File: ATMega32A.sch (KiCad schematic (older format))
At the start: 17 parts, among them J201 AVR-ISP-6, J202 UART, U201 ATmega32A-AU, Y201 16MHz

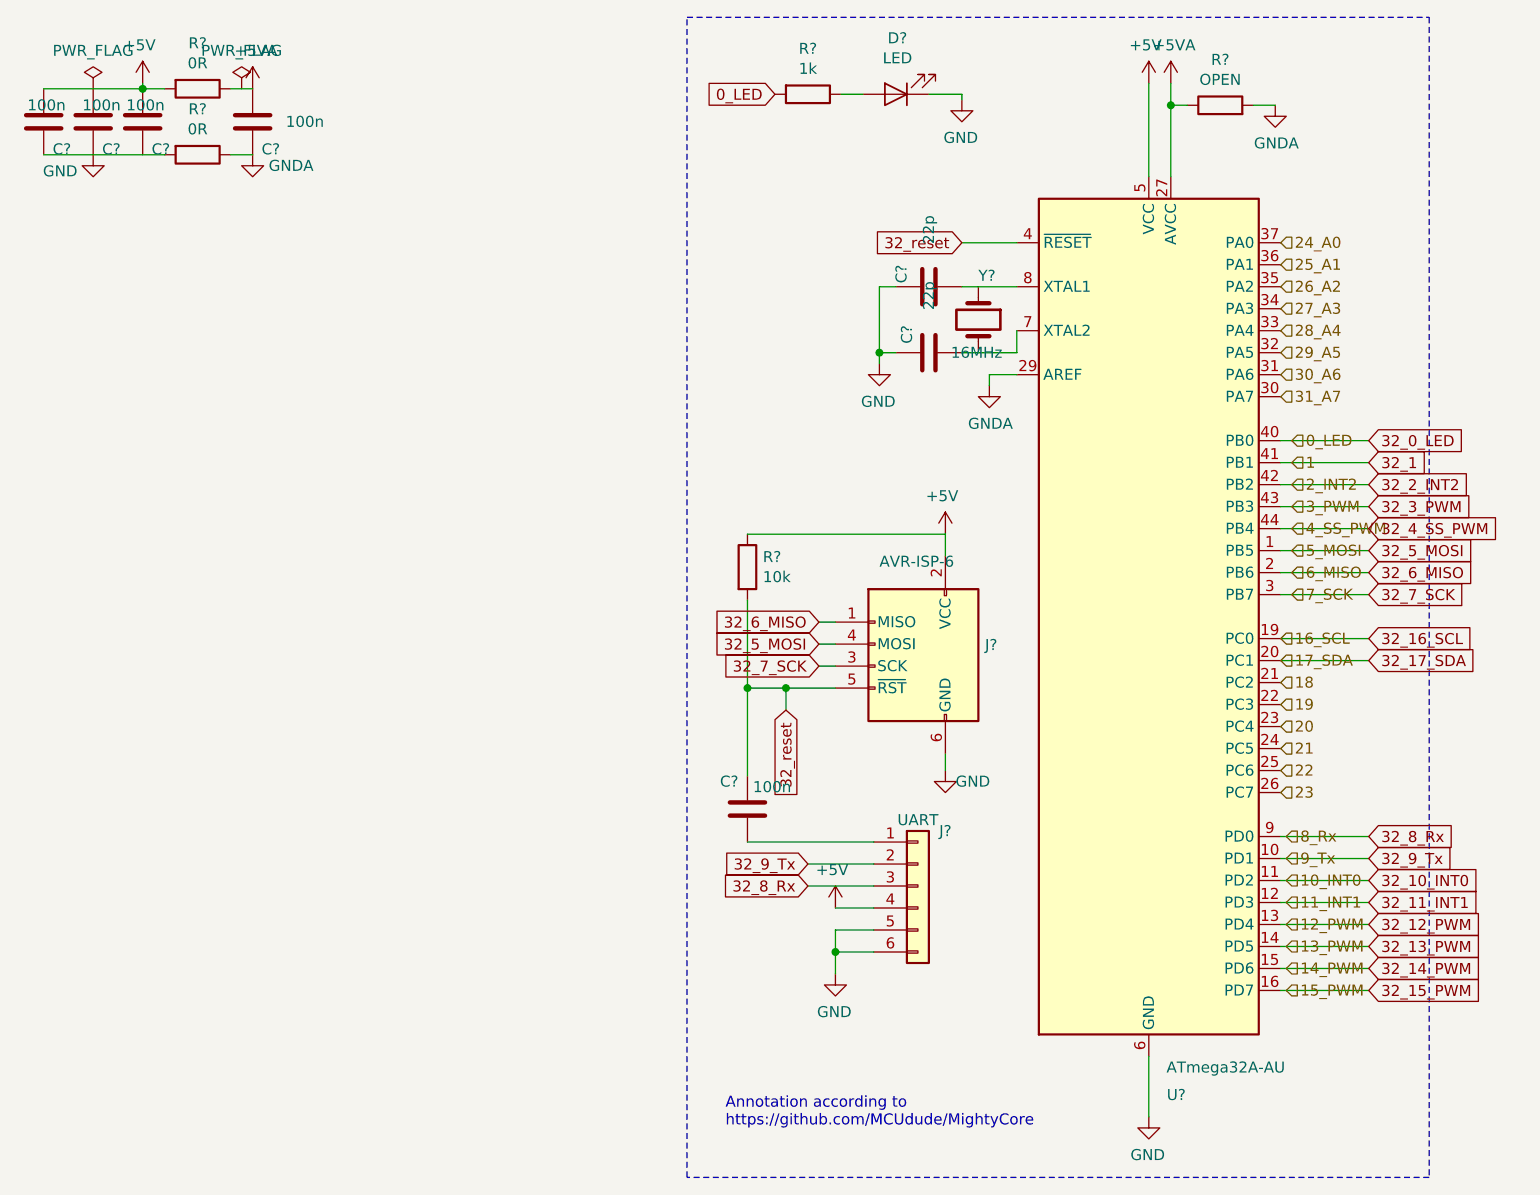
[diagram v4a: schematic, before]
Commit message: Intersheet cleanup
Footprints and cleanup naming on global labels between sheets
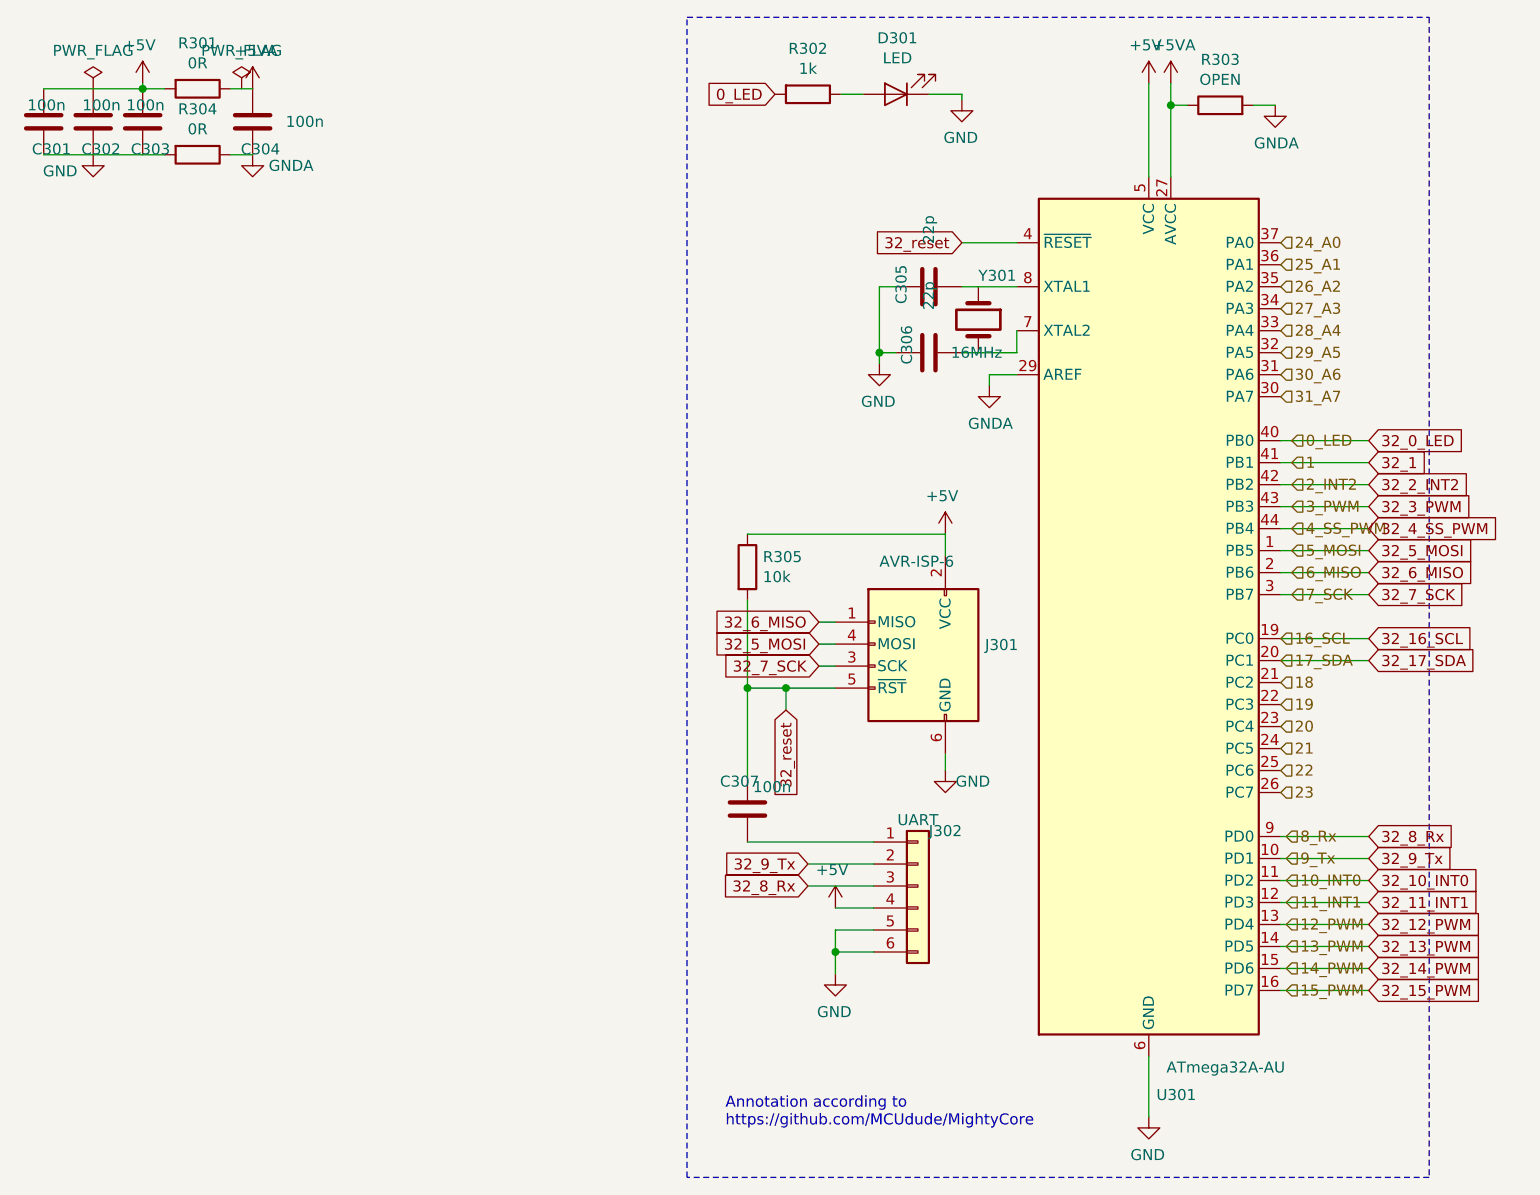
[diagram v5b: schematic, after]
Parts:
- renumbered C201 to C301, C202 to C302, C203 to C303, C204 to C304, C205 to C305, C206 to C306, C207 to C307, D201 to D301, J201 to J301, J202 to J302, R201 to R301, R202 to R302, R203 to R303, R204 to R304, R205 to R305, U201 to U301, Y201 to Y301

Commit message: LED and Xtal
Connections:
- net at C306.1, U301.7 (XTAL2): now also Y301.2
- net at C305.1, U301.8 (XTAL1): now also Y301.1
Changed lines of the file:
@@
 7_SCK
-Wire Wire Line
-	5400 2500 5650 2500
-Wire Wire Line
-	5400 2200 5650 2200
 Wire Wire Line
 	2075 1300 2175 1300
@@
 Wire Wire Line
 	1225 1600 1775 1600
+Wire Wire Line
+	5400 2500 5475 2500
+Connection ~ 5475 2500
+Wire Wire Line
+	5475 2500 5650 2500
+Wire Wire Line
+	5400 2200 5475 2200
+Connection ~ 5475 2200
+Wire Wire Line
+	5475 2200 5650 2200
 $EndSCHEMATC

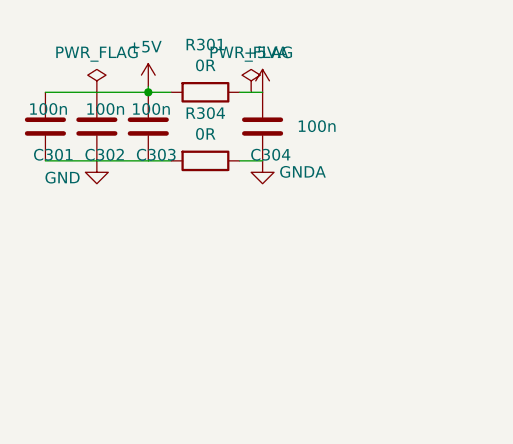
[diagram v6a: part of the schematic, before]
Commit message: ATMega 32 placed again - decoupling added
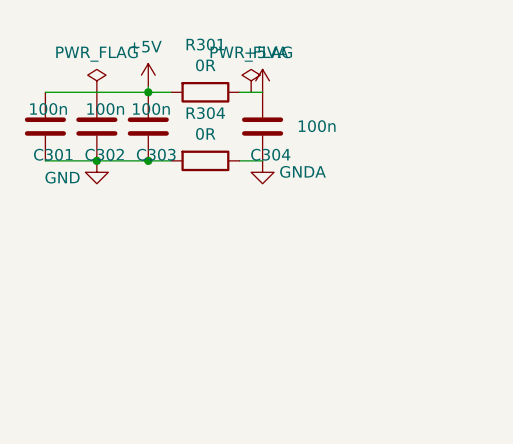
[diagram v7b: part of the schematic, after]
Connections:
- net GND: now also C301.1, C303.1, R304.2
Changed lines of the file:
@@
 	1225 1300 1675 1300
-Wire Wire Line
-	1225 1600 1775 1600
 Wire Wire Line
 	5400 2500 5475 2500
@@
 Wire Wire Line
 	5475 2200 5650 2200
+Wire Wire Line
+	1225 1600 1450 1600
+Connection ~ 1450 1600
+Wire Wire Line
+	1450 1600 1675 1600
+Connection ~ 1675 1600
+Wire Wire Line
+	1675 1600 1775 1600
 $EndSCHEMATC

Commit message: Routed
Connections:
- net +5V: now also C302.2
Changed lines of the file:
@@
 	2075 1300 2175 1300
 Wire Wire Line
-	1225 1300 1675 1300
+	1225 1300 1450 1300
 Wire Wire Line
 	5400 2500 5475 2500
@@
 Wire Wire Line
 	1675 1600 1775 1600
+Connection ~ 1450 1300
+Wire Wire Line
+	1450 1300 1675 1300
 $EndSCHEMATC
